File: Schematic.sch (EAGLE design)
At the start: 34 parts, among them IC1 LM339N, Q1 IRFZ48n, Q2 IRFZ48n, Q3 IRFZ48n, Q4 IRFZ48n, Q5 BC337, X1 12Vcc IN, X2 MOTOR DC

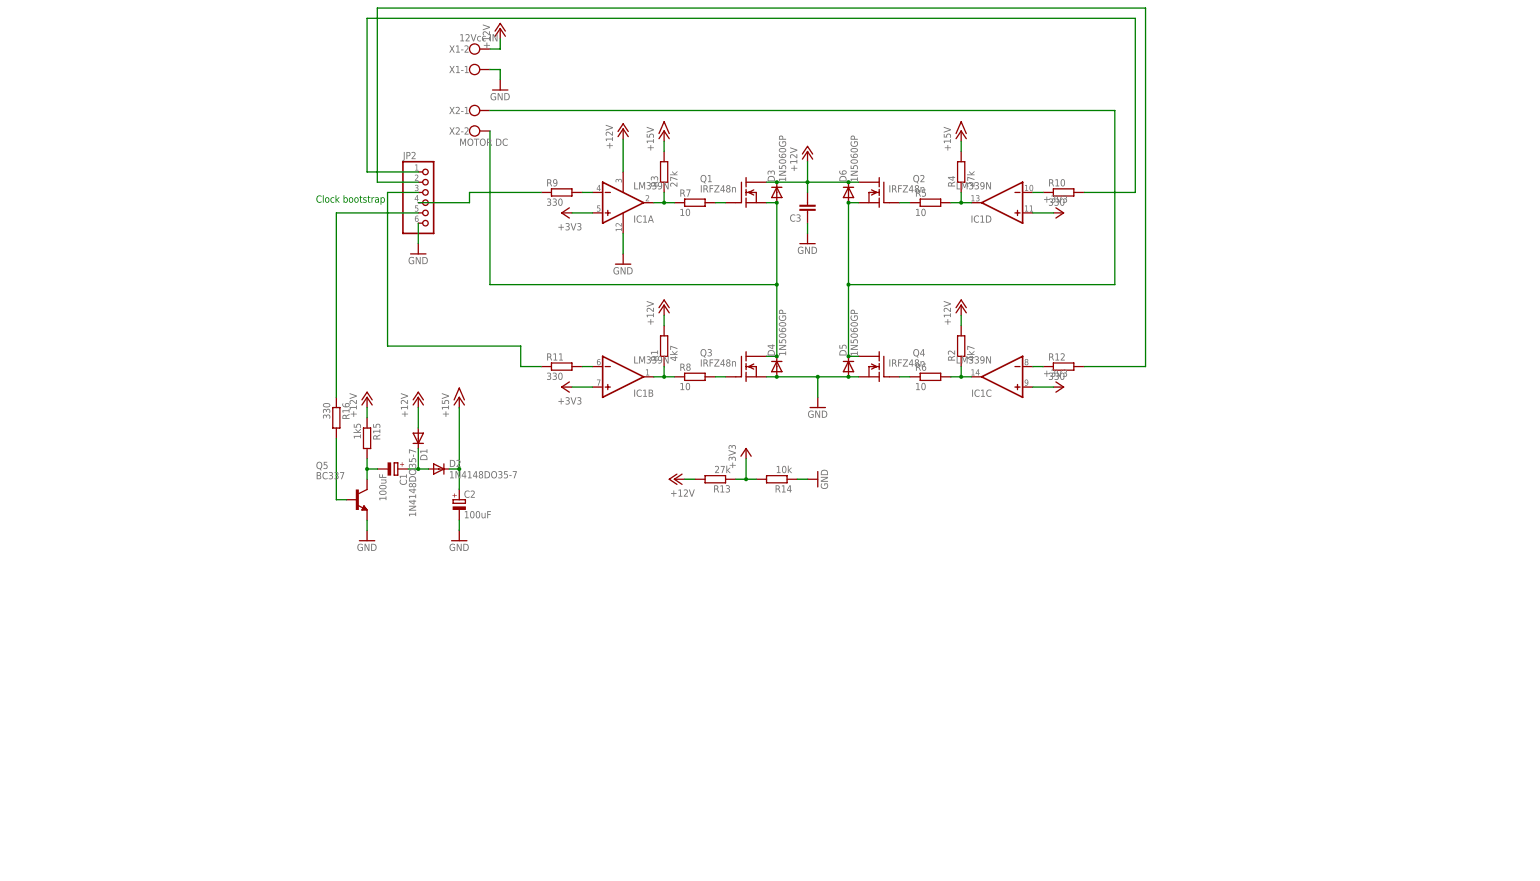
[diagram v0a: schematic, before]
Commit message: Ver 2
Board: A new design using a IC H bridge driver properly calculated for the motor and mosfets.
Algorithm: An algorithm that use a 3 axis gyro to balance itself.
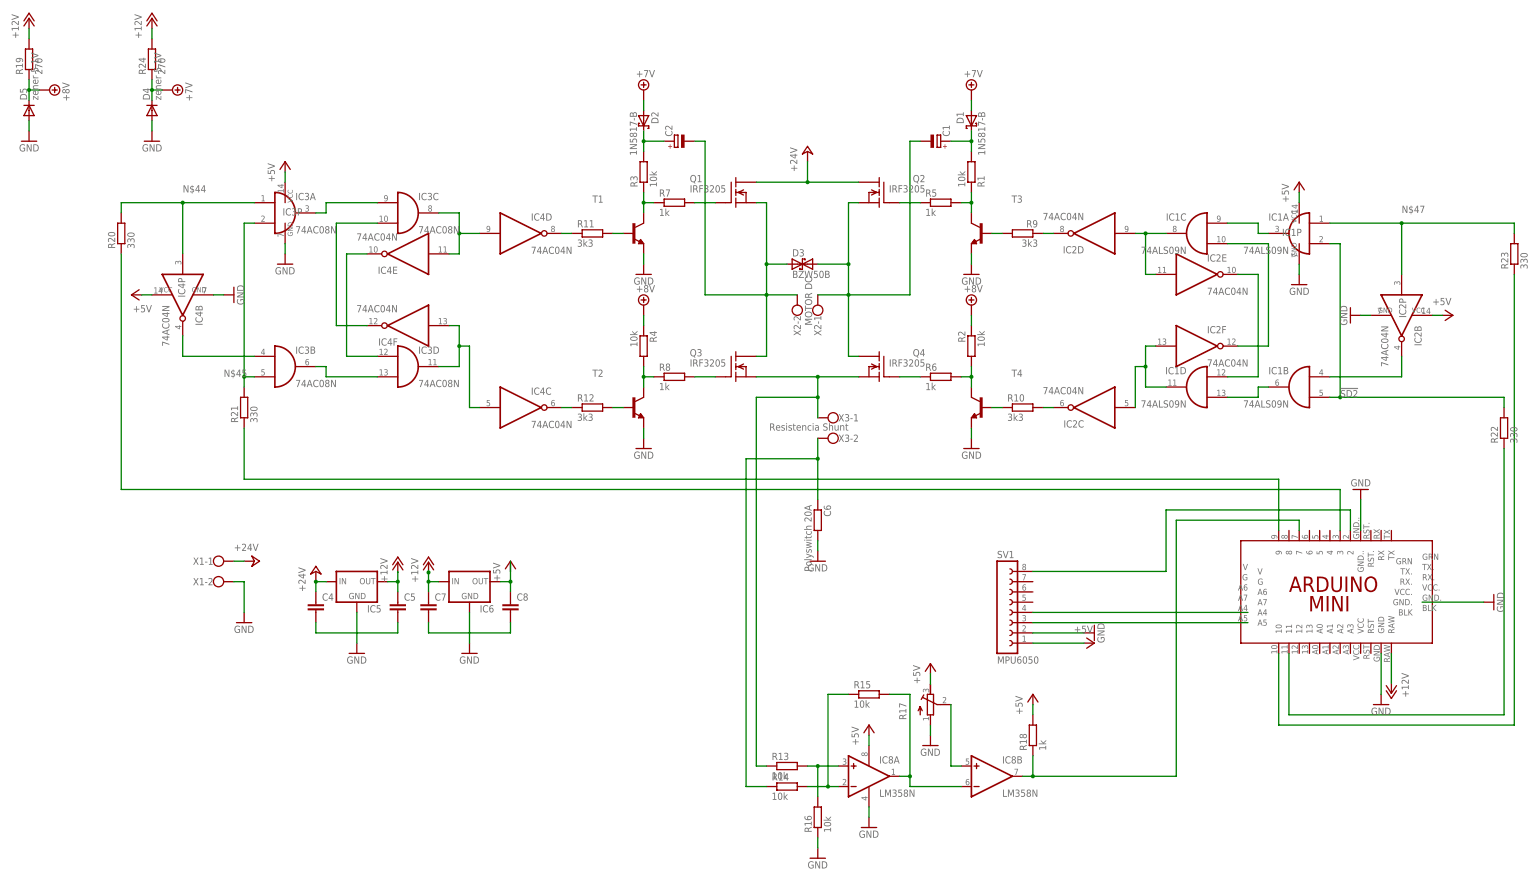
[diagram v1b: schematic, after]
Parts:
- removed C3: (no value), rcl:C-EU050-024X044
- removed D6: 1N5060GP, diode:1N5060GP
- removed JP2: (no value), pinhead:PINHD-1X6
- removed Q5: BC337, transistor-npn:BC337
- added C4, C5, C7, C8: (no value), rcl:C-EU050-024X044
- added C6: Polyswitch 20A, rcl:R-EU_0309/12
- added IC2, IC4: 74AC04N, 74xx-eu:74AC04N
- added IC3: 74AC08N, 74xx-eu:74AC08N
- added IC5, IC6: (no value), v-reg:78XXL
- added IC8: LM358N, linear:LM358N
- added R17: (no value), rcl:R-TRIMM64W
- added R18: 1k, rcl:R-EU_0204/7
- added R19, R24: 270, rcl:R-EU_0207/12
- added R20, R21, R22: 330, rcl:R-EU_0204/7
- added R23: 330, rcl:R-EU_0207/10
- added SV1: MPU6050, con-lsta:FE08-1
- added T1, T2, T3, T4: (no value), transistor:BC548-NPN-TO92-CBE
- added U$1: ARDUINO_MINI_PRO+AZUL, E14_Arduino_victor:ARDUINO_MINI_PRO+AZUL
- added X3: Resistencia Shunt, con-wago-500:W237-102
- C1, C2: value 100uF -> (none); device rcl:CPOL-EUE3.5-8 -> rcl:CPOL-EUE3.5-10
- D1, D2: value 1N4148DO35-7 -> 1N5817-B; device diode:1N4148DO35-7 -> diode:1N5817-B
- D3: value 1N5060GP -> BZW50B; device diode:1N5060GP -> diode:BZW50B
- D4, D5: value 1N5060GP -> zener 5.1V; device diode:1N5060GP -> diode:BYX90G
- IC1: value LM339N -> 74ALS09N; device linear:LM339N -> 74xx-eu:74ALS09N
- Q1, Q2, Q3, Q4: value IRFZ48n -> IRF3205; device transistor-fet:IRF510 -> transistor-fet:BUZ50A
- R1: value 4k7 -> 10k
- R10: value 330 -> 3k3; device rcl:R-EU_0207/7 -> rcl:R-EU_0207/12
- R11: value 330 -> 3k3
- R12: value 330 -> 3k3; device rcl:R-EU_0207/7 -> rcl:R-EU_0204/7
- R13, R3: value 27k -> 10k
- R15: value 1k5 -> 10k; device rcl:R-EU_0204/5 -> rcl:R-EU_0204/7
- R16: value 330 -> 10k; device rcl:R-EU_0207/7 -> rcl:R-EU_0204/7
- R2: value 4k7 -> 10k; device rcl:R-EU_0207/10 -> rcl:R-EU_0204/7
- R4: value 27k -> 10k; device rcl:R-EU_0207/10 -> rcl:R-EU_0204/7
- R5, R8: value 10 -> 1k; device rcl:R-EU_0207/7 -> rcl:R-EU_0204/7
- R6, R7: value 10 -> 1k; device rcl:R-EU_0207/10 -> rcl:R-EU_0204/7
- R9: value 330 -> 3k3; device rcl:R-EU_0204/7 -> rcl:R-EU_0207/15
- X1: value 12Vcc IN -> (none)
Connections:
- removed net +15V: C2.+, D2.C, R3.2, R4.2
- removed net +3V3: IC1A.+IN, IC1B.+IN, IC1C.+IN, IC1D.+IN, R13.1, R14.2
- removed net N$22: C1.-, Q5.C, R15.2
- removed net N$5: IC1C.OUT, R2.1, R6.2
- new net !SD1: R21.1, U$1.9
- new net !SD2: IC1A.I1, IC1B.I1, R22.2
- new net +24V: C4.1, IC5.IN, Q1.D, Q2.D, X1-1.KL
- new net +5V: C8.1, IC1P.VCC, IC2P.VCC, IC3P.VCC, IC4P.VCC, IC6.OUT, IC8P.V+, R17.E, R18.2, SV1.1
- new net +7V: D1.A, D2.A, D4.C, D5.C, R19.1, R2.1, R24.1, R4.1
- new net IN1: R20.1, U$1.3
- new net IN2: R23.1, U$1.10
- new net N$23: IC1B.I0, IC2B.O
- new net N$24: IC8B.+IN, R17.S
- new net N$25: R2.2, R6.2, T4.C
- new net N$26: R10.1, T4.B
- new net N$27: R4.2, R8.1, T2.C
- new net N$28: IC3D.O, IC4C.I, IC4F.I
- new net N$29: IC3D.I0, IC4E.O
- new net N$30: IC3C.I1, IC4F.O
- new net N$31: IC3A.O, IC3C.I0
- new net N$32: IC3B.O, IC3D.I1
- new net N$33: IC8A.+IN, R13.2, R16.2
- new net N$34: IC3B.I0, IC4B.O
- new net N$35: IC8A.-IN, R14.2, R15.1
- new net N$36: R3.1, R7.1, T1.C
- new net N$37: SV1.8, U$1.2
- new net N$38: IC8A.OUT, IC8B.-IN, R15.2
- new net N$39: R11.2, T1.B
- new net N$40: IC8B.OUT, R18.1, U$1.7
- new net N$41: R12.2, T2.B
- new net N$43: C6.1, R14.1, X3-2.KL
- new net N$44: IC3A.I0, IC4B.I, R20.2
- new net N$45: IC3A.I1, IC3B.I1, R21.2
- new net N$47: IC1A.I0, IC2B.I, R23.2
- new net N$49: R22.1, U$1.11
- new net N$53: IC2C.O, R10.2
- new net N$54: IC2D.O, R9.1
- new net N$55: IC4D.O, R11.1
- new net N$56: IC1D.O, IC2C.I, IC2F.I
- net +12V: now also C5.1, C7.1, IC5.OUT, IC6.IN, R19.2, R24.2, U$1.RAW; no longer C3.2, D1.A, D3.C, D6.C, IC1P.V+, Q1.D, Q2.D, R1.2, R13.2, R15.1, R2.2, X1-2.KL
- net GND: now also C4.2, C5.2, C6.2, C7.2, C8.2, IC2P.GND, IC3P.GND, IC4P.GND, IC5.GND, IC6.GND, IC8P.V-, R16.1, R17.A, SV1.2, T1.E, T2.E, T3.E, T4.E, U$1.GND, U$1.GND., U$1.GND.., X1-2.KL; no longer C2.-, C3.1, JP2.6, Q3.S, Q4.S, Q5.E, R14.1, X1-1.KL
- net N$1: now also C1.+, D1.C, R1.2; no longer IC1A.OUT, R3.1, R7.1
- net N$10: now also IC4C.O; no longer IC1C.-IN
- net N$12: now also R9.2, T3.B; no longer IC1B.-IN, R11.2
- net N$13: now also C2.-, D3.1; no longer D3.A, D4.C
- net N$14: now also IC1D.I0, IC2E.O; no longer JP2.4, R9.1
- net N$15: now also SV1.3, U$1.A5; no longer JP2.1, R10.2
- net N$16: now also C1.-, D3.2; no longer D5.C, D6.A
- net N$17: now also IC1C.I1, IC2F.O; no longer JP2.3, R11.1
- net N$18: now also Q3.S, Q4.S, R13.1, X3-1.KL; no longer JP2.2, R12.2
- net N$19: now also IC1B.O, IC1D.I1; no longer C1.+, D1.C, D2.A
- net N$2: now also C2.+, D2.C, R3.2; no longer IC1D.OUT, R4.1, R5.2
- net N$20: now also IC1A.O, IC1C.I0; no longer Q5.B, R16.2
- net N$21: now also SV1.4, U$1.A4; no longer JP2.5, R16.1
- net N$6: now also IC3C.O, IC4D.I, IC4E.I; no longer IC1B.OUT, R1.1, R8.1
- net N$7: now also R1.1, R5.2, T3.C; no longer IC1A.-IN, R9.2
- net N$8: now also IC1C.O, IC2D.I, IC2E.I; no longer IC1D.-IN, R10.1
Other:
- note added: "NOTAS IMPORTANTES: *Los transistores de la base de los fets tienen q ser tipo BC548.. Puede q mas adelante haya q reemplazarlos por fets chiquitos. *Hay q regular bien la tension de los transistores de gate para q qde limitado en corriente. *Chequear pero parece q las AND estas son OPEN-COLLECTOR.. Hay q cambiarlas por las comunes q son 08. *Hay q agregar la entrada del medidor de corriente al ar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"
- note removed: "Clock bootstrap"
- moved on the sheet: C1, C2, D4, D5, Q1, Q3, R1, R10, R11, R12, R13, R14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

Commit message: Ver 3
Board: Some adjustments at the design.
Algorithm:  Adjustments too.
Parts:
- removed IC3: 74AC08N, 74xx-eu:74AC08N
- removed IC4: 74AC04N, 74xx-eu:74AC04N
- removed IC5, IC6: (no value), v-reg:78XXL
- removed IC8: LM358N, linear:LM358N
- removed R18: 1k, rcl:R-EU_0204/7
- removed R19, R24: 270, rcl:R-EU_0207/12
- removed R20, R21, R22: 330, rcl:R-EU_0204/7
- removed R23: 330, rcl:R-EU_0207/10
- removed T1, T2, T3, T4: (no value), transistor:BC548-NPN-TO92-CBE
- removed X3: Resistencia Shunt, con-wago-500:W237-102
- added C3: (no value), rcl:C-EU050-030X075
- added D6, D7, D8: 1N4148DO35-10, diode:1N4148DO35-10
- added D9: 15KEXXC, diode:15KEXXC
- added JP1: (no value), pinhead:PINHD-1X6
- added SJ1: (no value), jumper:SJW
- added U$2, U$3: IR2104, IR2104:IR2104
- C1: value (none) -> 1uF; device rcl:CPOL-EUE3.5-10 -> rcl:CPOL-EUE3.5-8
- C2: value (none) -> 220nF; device rcl:CPOL-EUE3.5-10 -> rcl:C-EU075-032X103
- C4: device rcl:C-EU050-024X044 -> rcl:CPOL-EUE3.5-8
- C5: value (none) -> 220nF; device rcl:C-EU050-024X044 -> rcl:C-EU075-032X103
- C6: device rcl:R-EU_0309/12 -> rcl:C-US075-032X103
- C7: value (none) -> 330nF
- C8: value (none) -> 100nF
- D1, D2: value 1N5817-B -> 1N4148DO35-10; device diode:1N5817-B -> diode:1N4148DO35-10
- D3: value BZW50B -> 1N4148DO35-10; device diode:BZW50B -> diode:1N4148DO35-10
- D4, D5: value zener 5.1V -> 1N4148DO35-10; device diode:BYX90G -> diode:1N4148DO35-10
- IC1: value 74ALS09N -> (none); device 74xx-eu:74ALS09N -> v-reg:78XXL
- IC2: value 74AC04N -> LM358N; device 74xx-eu:74AC04N -> linear:LM358N
- Q1, Q2, Q3, Q4: device transistor-fet:BUZ50A -> transistor-fet Victor:BUZ10
- R1, R2, R3: value 10k -> 330
- R10: value 3k3 -> (none); device rcl:R-EU_0207/12 -> rcl_Victor:R-EU_0204/7
- R11, R12: value 3k3 -> (none); device rcl:R-EU_0204/7 -> rcl_Victor:R-EU_0204/7
- R13, R4: value 10k -> (none); device rcl:R-EU_0204/7 -> rcl_Victor:R-EU_0204/7
- R14: value 10k -> (none); device rcl:R-EU_0204/7 -> rcl_Victor:R-TRIMM64W
- R15: value 10k -> RESISTENCIA SHUNT; device rcl:R-EU_0204/7 -> resistor:R-EU_0922V
- R16: value 10k -> 1k; device rcl:R-EU_0204/7 -> rcl:R-EU_0207/10
- R17: value (none) -> 1k; device rcl:R-TRIMM64W -> rcl:R-EU_0207/10
- R5: value 1k -> 10; device rcl:R-EU_0204/7 -> rcl:R-EU_0207/12
- R6, R7: value 1k -> 10; device rcl:R-EU_0204/7 -> rcl:R-EU_0207/10
- R8: value 1k -> 10; device rcl:R-EU_0204/7 -> rcl:R-EU_0207/15
- R9: value 3k3 -> 330; device rcl:R-EU_0207/15 -> rcl:R-EU_0207/10
- X1: value (none) -> 12Vcc IN
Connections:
- removed net !SD1: R21.1, U$1.9
- removed net !SD2: IC1A.I1, IC1B.I1, R22.2
- removed net +7V: D1.A, D2.A, D4.C, D5.C, R19.1, R2.1, R24.1, R4.1
- removed net IN1: R20.1, U$1.3
- removed net IN2: R23.1, U$1.10
- removed net N$12: R9.2, T3.B
- removed net N$14: IC1D.I0, IC2E.O
- removed net N$17: IC1C.I1, IC2F.O
- removed net N$29: IC3D.I0, IC4E.O
- removed net N$30: IC3C.I1, IC4F.O
- removed net N$35: IC8A.-IN, R14.2, R15.1
- removed net N$36: R3.1, R7.1, T1.C
- removed net N$38: IC8A.OUT, IC8B.-IN, R15.2
- removed net N$39: R11.2, T1.B
- removed net N$40: IC8B.OUT, R18.1, U$1.7
- removed net N$41: R12.2, T2.B
- removed net N$43: C6.1, R14.1, X3-2.KL
- removed net N$44: IC3A.I0, IC4B.I, R20.2
- removed net N$45: IC3A.I1, IC3B.I1, R21.2
- removed net N$47: IC1A.I0, IC2B.I, R23.2
- removed net N$49: R22.1, U$1.11
- removed net N$53: IC2C.O, R10.2
- removed net N$54: IC2D.O, R9.1
- removed net N$55: IC4D.O, R11.1
- removed net N$56: IC1D.O, IC2C.I, IC2F.I
- new net N$22: IC2A.OUT, IC2B.-IN, R11.2
- new net N$48: JP1.6, U$1.BLK
- new net N$5: R2.2, U$3.IN
- new net N$50: JP1.3, U$1.RX.
- new net N$51: JP1.2, U$1.TX.
- new net N$52: JP1.1, U$1.GRN
- net +12V: now also C1.+, C4.+, C8.1, D1.A, D2.A, IC1.OUT, SJ1.2, U$2.VCC, U$3.VCC; no longer C5.1, C7.1, IC5.OUT, IC6.IN, R19.2, R24.2
- net +24V: now also C3.2, C7.1, IC1.IN, SJ1.1, X1-2.KL; no longer C4.1, IC5.IN, X1-1.KL
- net +5V: now also IC2P.V+, JP1.4, R12.2, R14.E, U$1.VCC.; no longer C8.1, IC1P.VCC, IC2P.VCC, IC3P.VCC, IC4P.VCC, IC6.OUT, IC8P.V+, R17.E, R18.2
- net GND: now also C1.-, C3.1, C4.-, IC1.GND, IC2P.V-, JP1.5, R13.1, R14.A, U$2.COM, U$3.COM, X1-1.KL; no longer C4.2, C5.2, D4.A, D5.A, IC1P.GND, IC2P.GND, IC3P.GND, IC4P.GND, IC5.GND, IC6.GND, IC8P.V-, R16.1, R17.A, T1.E, T2.E, T3.E, T4.E, X1-2.KL
- net N$1: now also R9.2, U$2.IN; no longer C1.+, D1.C, R1.2
- net N$10: now also R9.1, U$1.3; no longer IC4C.O, R12.1
- net N$11: now also D8.A, Q4.G; no longer Q3.G
- net N$13: now also C2.2, D9.1, R16.1, U$2.VS; no longer C2.-, D3.1
- net N$16: now also C5.2, D9.2, R17.1, U$3.VS; no longer C1.-, D3.2
- net N$18: now also R15.2, R4.1; no longer R13.1, X3-1.KL
- net N$19: now also R2.1, U$1.10; no longer IC1B.O, IC1D.I1
- net N$2: now also C2.1, D1.C, U$2.VB; no longer C2.+, D2.C, R3.2
- net N$20: now also C5.1, D2.C, U$3.VB; no longer IC1A.O, IC1C.I0
- net N$23: now also D5.C, R7.1, U$2.HO; no longer IC1B.I0, IC2B.O
- net N$24: now also D7.C, R6.2, U$2.LO; no longer IC8B.+IN, R17.S
- net N$25: now also D8.C, R8.1, U$3.LO; no longer R2.2, R6.2, T4.C
- net N$26: now also D6.C, R5.2, U$3.HO; no longer R10.1, T4.B
- net N$27: now also IC2A.+IN, R13.2; no longer R8.1, T2.C
- net N$28: now also D3.A, R1.2, U$2.SD; no longer IC3D.O, IC4C.I, IC4F.I
- net N$3: now also D5.A, R16.2
- net N$31: now also IC2A.-IN, R10.2, R11.1; no longer IC3A.O, IC3C.I0
- net N$32: now also IC2B.+IN, R14.S; no longer IC3B.O, IC3D.I1
- net N$33: now also R3.1, U$1.11; no longer IC8A.+IN, R13.2, R16.2
- net N$34: now also C6.1, R10.1, R15.1; no longer IC3B.I0, IC4B.O
- net N$4: now also D6.A, R17.2
- net N$6: now also D4.A, R3.2, U$3.SD; no longer IC3C.O, IC4D.I, IC4E.I
- net N$7: now also U$1.9; no longer R5.2, T3.C
- net N$8: now also D3.C, D4.C, IC2B.OUT, R12.1; no longer IC1C.O, IC2D.I, IC2E.I
- net N$9: now also D7.A, Q3.G; no longer Q4.G
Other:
- note removed: "NOTAS IMPORTANTES: *Los transistores de la base de los fets tienen q ser tipo BC548.. Puede q mas adelante haya q reemplazarlos por fets chiquitos. *Hay q regular bien la tension de los transistores de gate para q qde limitado en corriente. *Chequear pero parece q las AND estas son OPEN-COLLECTOR.. Hay q cambiarlas por las comunes q son 08. *Hay q agregar la entrada del medidor de corriente al ar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"
- moved on the sheet: C1, C5, C6, C7, C8, Q1, Q3, Q4, R1, R10, R11, R12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
